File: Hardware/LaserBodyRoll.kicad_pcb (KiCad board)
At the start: 2 copper layers, 65 x 30 mm, 49 parts, among them J1 Conn_02x13_Odd_Even, J2 Conn_01x08, Q1 Q_NPN_BCE, U1 AOZ1280CI, U2 ITS42K5D, U3 MCP47X, U4 ICM-20602, U5 MCP25625, U6 VL53L0X, U7 LD3985, Y1 16MHz

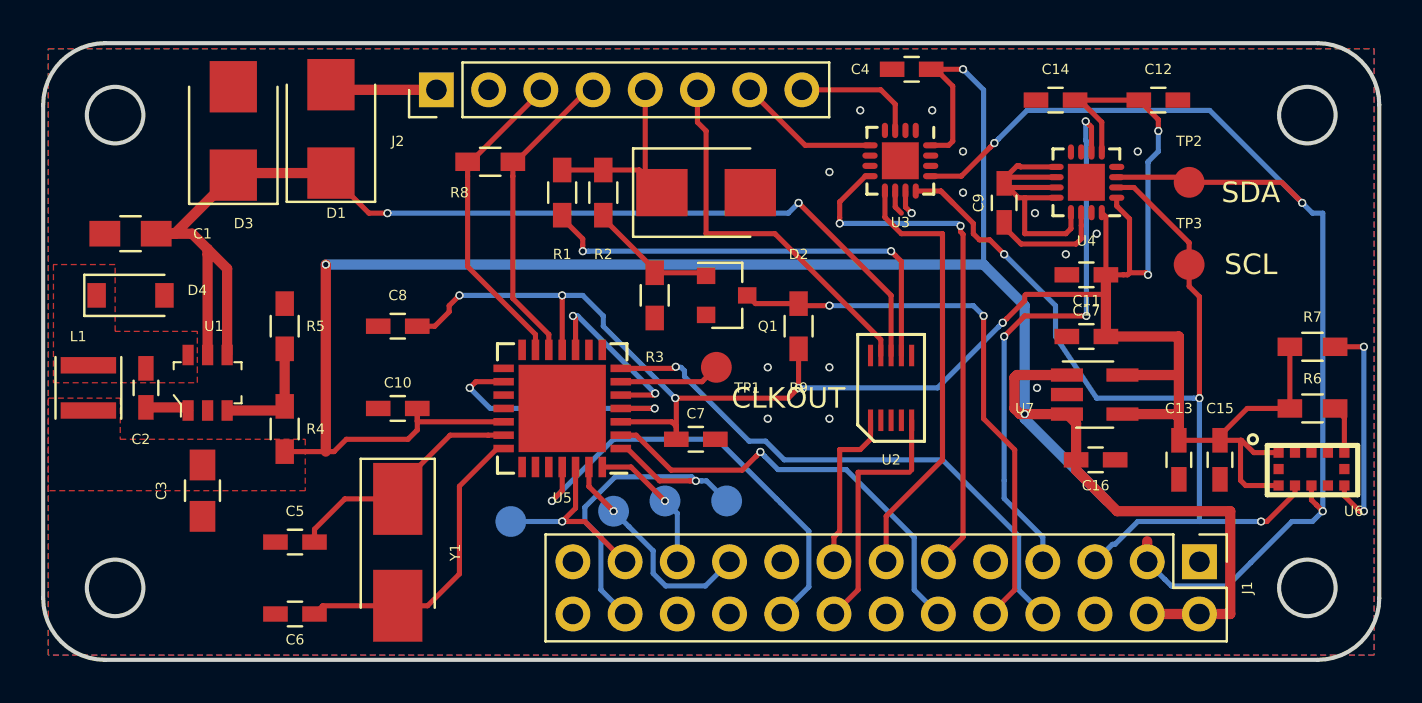
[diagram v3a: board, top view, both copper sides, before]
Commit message: Fixed problems on the board and added LEDs.
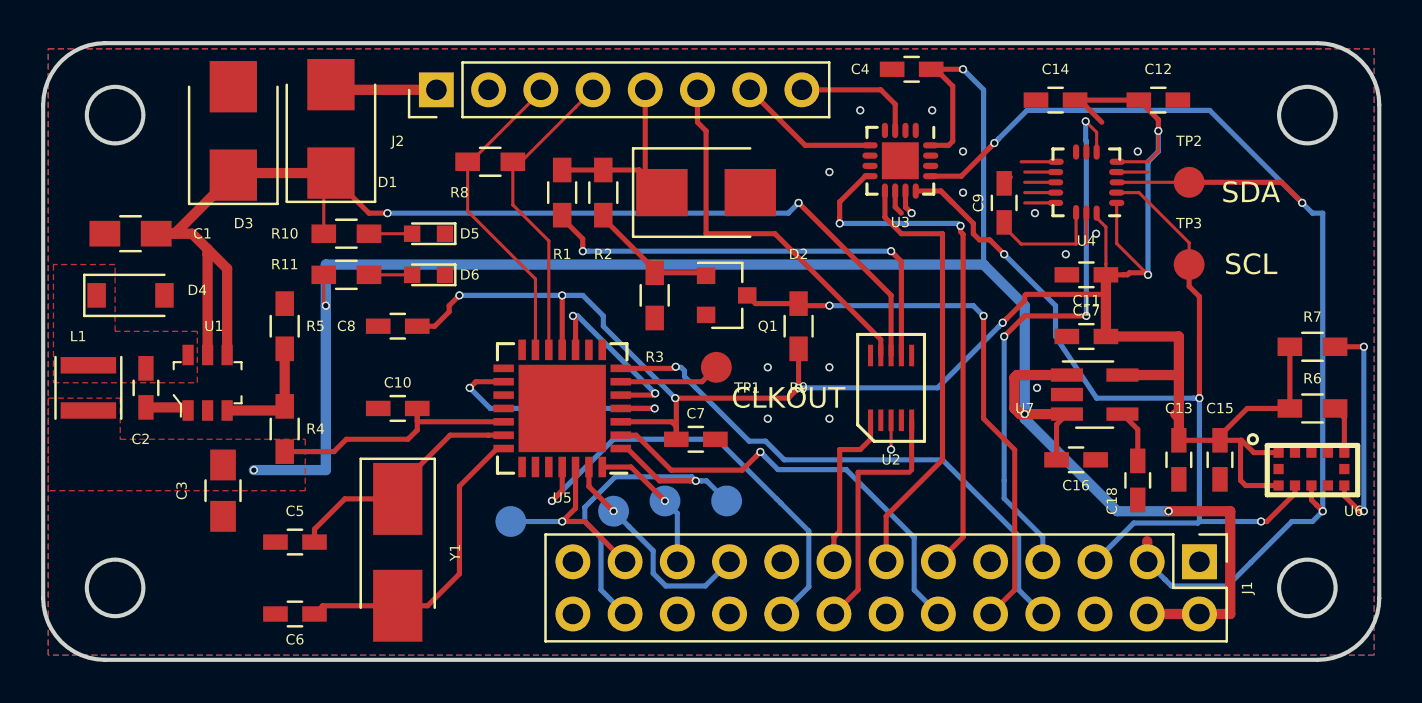
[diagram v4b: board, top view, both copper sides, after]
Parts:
- added C18: 0.1u, Capacitors_SMD:C_0603_HandSoldering, F.Cu at (108.0, 58.5)
- added D5: LED, LEDs:LED_0603, F.Cu at (73.5, 46.5)
- added D6: LED, LEDs:LED_0603, F.Cu at (73.5, 48.5)
- added R10: 600, Resistors_SMD:R_0603_HandSoldering, F.Cu at (69.5, 46.5)
- added R11: 250, Resistors_SMD:R_0603_HandSoldering, F.Cu at (69.5, 48.5)
- C17: value 0.1u -> 1u
- U4: footprint Housings_DFN_QFN:QFN-16-1EP_3x3mm_Pitch0.5mm -> KicadFootprint:QFN-16-no_center_3x3mm_Pitch0.5mm
- moved C3 1.00 mm to (63.5, 59.0)
- moved C16 0.95 mm to (105.0, 57.5)
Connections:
- U5 pad 15: Net-(U5-Pad15) -> GND
- U7 pad 4: VCC -> Net-(C18-Pad2)
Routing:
- net +5V: track 111.6 -> 114.9 mm, vias 3 -> 5
- net 12V: track 56.3 -> 59.4 mm
- net GND: track 18.4 -> 15.5 mm, vias 15 -> 16
- net Net-(C18-Pad2): track 0.00 -> 2.58 mm
- net Net-(D6-Pad2): track 0.00 -> 2.10 mm
- net Net-(D5-Pad2): track 0.00 -> 2.10 mm
- net VCC: track 107.7 -> 107.2 mm
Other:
- board text added: "LaserBodyRoll Rev E Copyright Nick Butts 2019"
- board text removed: "LaserBodyRoll Rev D Copyright Nick Butts 2019"
